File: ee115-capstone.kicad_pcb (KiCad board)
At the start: 2 copper layers, 122 parts, among them J1 2171790001, J2 9V_BATTERY, J3 Conn_01x04_Pin, J5 Conn_01x03_Pin, J6 Conn_02x02_Odd_Even, Q1 PMOS, Q2 NMOS, Q3 NPN, Q4 AO3400A, Q5 AO3400A, Q6 NMOS, SW1 SW_Push, SW2 SW_Push, SW3 SW_Push, U1 OPA2140AIDR, U10 SN74LVC1G02DCKR (NOR), U11 SN74LVC1G02DCKR (NOR), U12 ALD1107PBL, U13 MCP6571T-E/OT, U14 SL78L05, U15 300P14-U, U16 OPA705PA, U17 MIC4605-2YM-TR, U18 OPA705PA, U19 OPA705PA, U2 CD4052BPWR, U20 TLV9101IDBVR, U21 MCP6571T-E/OT, U3 LM393DR, U4 ADG601BRMZ-REEL7, U5 ESP32-C3-WROOM-02-N4, U6 AP2112K-3.3, U7 MCP601T-E_OT, U8 MCP6571T-E/OT, U9 MCP6571T-E/OT

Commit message: adc PCB
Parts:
- removed R8: 0, Resistor_SMD:R_0805_2012Metric
- added U13: MCP6571T-E/OT, footprints:SOP_MCP6571T-E&slash_OT_MCH, F.Cu at (113.8, 56.3)
- moved C4 111.4 mm to (156.8, 62.4), turned to 90 degrees
- moved R2 107.2 mm to (154.6, 67.0), turned to -90 degrees
- moved C2 105.3 mm to (151.5, 54.8)
- moved R3 104.5 mm to (154.7, 63.3), turned to -90 degrees
- moved C16 103.5 mm to (155.0, 59.5), turned to 180 degrees
- moved J6 100.8 mm to (154.2, 75.1), turned to -90 degrees
- moved U1 100.1 mm to (149.2, 63.8)
- moved D1 98.9 mm to (155.8, 54.8), turned to 90 degrees
- moved U4 98.8 mm to (136.6, 63.0), turned to 90 degrees
- moved R1 97.2 mm to (144.1, 62.5), turned to -90 degrees
- moved C6 92.2 mm to (139.4, 54.5), turned to 90 degrees
- moved J1 90.7 mm to (154.4, 46.0), turned to 90 degrees
- moved R10 90.6 mm to (151.8, 52.2), turned to 180 degrees
- moved J5 90.0 mm to (126.2, 29.5), turned to 180 degrees
- moved R9 87.5 mm to (151.7, 39.6), turned to 180 degrees
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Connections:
- C23 pad 1: +3V3 -> /LDO/+3.3V
- C24 pad 1: +3V3 -> /LDO/+3.3V
- Q6 pad 3: +3V3 -> /LDO/+3.3V
- R36 pad 1: +3V3 -> /LDO/+3.3V
- R38 pad 1: +3V3 -> /LDO/+3.3V
- U19 pad 7: unconnected-(U19-V+-Pad7) -> +9V
- U21 pad 6: (no net) -> +5V
- U5 pad 10: /ADC-MCU/COMP_OUT -> /ADC-MCU/MUX_B
- U5 pad 11: /ADC-MCU/MUX_B -> /ADC-MCU/MUX_A
- U5 pad 17: /ADC-MCU/ESP_ADC_2 -> /Thermistor
- U5 pad 6: /ADC-MCU/MUX_A -> /ADC-MCU/COMP_OUT
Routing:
- net 1.65V: track 0.00 -> 62.9 mm
- net /Thermopile: track 0.00 -> 56.4 mm, vias 0 -> 2
- net /Thermistor: track 0.00 -> 39.8 mm, vias 0 -> 1
- net /ADC-MCU/ESP_ADC_1: track 0.00 -> 29.3 mm, vias 0 -> 2
- net GND: track 0.00 -> 26.8 mm, vias 0 -> 5
- net Net-(U1-OUTA): track 0.00 -> 26.3 mm, vias 0 -> 2
- net /ADC-MCU/SCL: track 0.00 -> 19.0 mm
- net /ADC-MCU/COMP_OUT_BAR: track 0.00 -> 18.9 mm, vias 0 -> 2
- net /ADC-MCU/SDA: track 0.00 -> 18.8 mm
- net /ADC-MCU/BOOT: track 0.00 -> 17.8 mm, vias 0 -> 1
- net +3V3: track 0.00 -> 17.3 mm, vias 0 -> 3
- net /ADC-MCU/-VREF: track 0.00 -> 16.5 mm
- net /RANGE_SEL: track 0.00 -> 16.1 mm
- net Net-(U1-INA-): track 0.00 -> 15.7 mm
- net /ADC-MCU/EN: track 0.00 -> 14.0 mm
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- added copper zone on F.Cu, net +5V
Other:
- copper layers 2 -> 4

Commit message: pcb layout
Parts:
- removed U13 (x2): MCP6571T-E/OT, footprints:SOP_MCP6571T-E&slash_OT_MCH
- added C25: C_Polarized, Capacitor_SMD:C_0805_2012Metric, F.Cu at (179.7, 109.5)
- added C26: C_Polarized, Capacitor_SMD:C_0805_2012Metric, F.Cu at (171.3, 183.9)
- added C27: C_Polarized, Capacitor_SMD:C_0805_2012Metric, F.Cu at (171.3, 180.9)
- added C28: C_Polarized, Capacitor_SMD:C_0805_2012Metric, F.Cu at (171.4, 178.0)
- added C29: C_Polarized, Capacitor_SMD:C_0805_2012Metric, F.Cu at (171.4, 175.2)
- added C30: C_Polarized, Capacitor_SMD:C_0805_2012Metric, F.Cu at (158.3, 162.8)
- added C31: C_Polarized, Capacitor_SMD:C_0805_2012Metric, F.Cu at (158.3, 165.7)
- added C32: C_Polarized, Capacitor_SMD:C_0805_2012Metric, F.Cu at (158.3, 168.5)
- added C33: C_Polarized, Capacitor_SMD:C_0805_2012Metric, F.Cu at (158.3, 171.4)
- added C34: C_Polarized, Capacitor_SMD:C_0805_2012Metric, F.Cu at (154.7, 161.3)
- added C35: C_Polarized, Capacitor_SMD:C_0805_2012Metric, F.Cu at (154.7, 164.2)
- added C36: C_Polarized, Capacitor_SMD:C_0805_2012Metric, F.Cu at (154.7, 167.0)
- added C37: C_Polarized, Capacitor_SMD:C_0805_2012Metric, F.Cu at (154.7, 169.9)
- added C38: C_Polarized, Capacitor_SMD:C_0805_2012Metric, F.Cu at (137.7, 164.0)
- added C39: C_Polarized, Capacitor_SMD:C_0805_2012Metric, F.Cu at (161.9, 173.2)
- added C40: C_Polarized, Capacitor_SMD:C_0805_2012Metric, F.Cu at (146.8, 157.8)
- added C41: C_Polarized, Capacitor_SMD:C_0805_2012Metric, F.Cu at (88.5, 181.2)
- added C42: C_Polarized, Capacitor_SMD:C_0805_2012Metric, F.Cu at (153.4, 151.8)
- added C43: C_Polarized, Capacitor_SMD:C_0805_2012Metric, F.Cu at (88.5, 187.2)
- added C44: C_Polarized, Capacitor_SMD:C_0805_2012Metric, F.Cu at (88.5, 190.2)
- added C45: C_Polarized, Capacitor_SMD:C_0805_2012Metric, F.Cu at (147.8, 115.6)
- added C46: C_Polarized, Capacitor_SMD:C_0805_2012Metric, F.Cu at (95.0, 192.2)
- added C47: C_Polarized, Capacitor_SMD:C_0805_2012Metric, F.Cu at (95.0, 195.2)
- added C48: C_Polarized, Capacitor_SMD:C_0805_2012Metric, F.Cu at (143.3, 178.1)
- added C49: C_Polarized, Capacitor_SMD:C_0805_2012Metric, F.Cu at (140.0, 178.1)
- added D4: D_Schottky, Diode_SMD:D_SOD-523, F.Cu at (165.4, 148.1)
- added Q7: PNP, Package_TO_SOT_THT:TO-220F-3_Vertical, F.Cu at (166.6, 155.6)
- added Q8: NPN, Package_TO_SOT_THT:TO-220-3_Horizontal_TabDown, F.Cu at (175.3, 104.7)
- added R30: R, Resistor_SMD:R_0805_2012Metric, F.Cu at (166.9, 176.3)
- added R42: R, Resistor_SMD:R_0805_2012Metric, F.Cu at (166.7, 150.1)
- added R43: R, Resistor_SMD:R_0805_2012Metric, F.Cu at (172.2, 160.8)
- added R44: R, Resistor_SMD:R_0805_2012Metric, F.Cu at (172.2, 157.2)
- added R45: R, Resistor_SMD:R_0805_2012Metric, F.Cu at (176.4, 108.3)
- added R46: R, Resistor_SMD:R_0805_2012Metric, F.Cu at (162.7, 183.9)
- added R47: R, Resistor_SMD:R_0805_2012Metric, F.Cu at (162.7, 180.9)
- added R48: R, Resistor_SMD:R_0805_2012Metric, F.Cu at (162.7, 178.0)
- added R50: R, Resistor_SMD:R_0805_2012Metric, F.Cu at (162.7, 186.8)
- added R51: R, Resistor_SMD:R_0805_2012Metric, F.Cu at (158.4, 185.4)
- added R52: R, Resistor_SMD:R_0805_2012Metric, F.Cu at (158.4, 183.0)
- added R53: R, Resistor_SMD:R_0805_2012Metric, F.Cu at (158.4, 180.7)
- added R54: R, Resistor_SMD:R_0805_2012Metric, F.Cu at (158.4, 178.3)
- added R8: R, Resistor_SMD:R_0805_2012Metric, F.Cu at (162.8, 153.5)
- added Re1: R, Resistor_SMD:R_0805_2012Metric, F.Cu at (161.8, 161.3)
- added Re2: R, Resistor_SMD:R_0805_2012Metric, F.Cu at (161.8, 164.2)
- added Re3: R, Resistor_SMD:R_0805_2012Metric, F.Cu at (161.8, 167.0)
- added Re4: R, Resistor_SMD:R_0805_2012Metric, F.Cu at (161.8, 169.9)
- added TP19: TestPoint, TestPoint:TestPoint_Plated_Hole_D2.0mm, F.Cu at (146.4, 151.1)
- added TP20: TestPoint, TestPoint:TestPoint_Plated_Hole_D2.0mm, F.Cu at (142.8, 149.2)
- added TP21: TestPoint, TestPoint:TestPoint_Plated_Hole_D2.0mm, F.Cu at (148.5, 154.1)
- added TP22: TestPoint, TestPoint:TestPoint_Plated_Hole_D2.0mm, F.Cu at (144.2, 145.7)
- added TP23: TestPoint, TestPoint:TestPoint_Plated_Hole_D2.0mm, F.Cu at (165.4, 143.0)
- added TP24: TestPoint, TestPoint:TestPoint_Plated_Hole_D2.0mm, F.Cu at (139.5, 151.9)
- added TP26: TestPoint, TestPoint:TestPoint_Plated_Hole_D2.0mm, F.Cu at (159.2, 154.2)
- Q3: footprint Package_TO_SOT_THT:TO-220-3_Horizontal_TabDown -> Package_TO_SOT_THT:TO-220-3_Vertical
- TP1, TP2, TP3, TP4, TP5, TP6, TP7, TP8: footprint Connector_Pin:Pin_D1.0mm_L10.0mm -> TestPoint:TestPoint_Plated_Hole_D2.0mm
- TP10, TP11, TP12, TP13, TP14, TP15, TP16, TP17, TP18, TP9: footprint TestPoint:TestPoint_Pad_D1.0mm -> TestPoint:TestPoint_Plated_Hole_D2.0mm
- U10, U11: footprint footprints:DCK0005A_N -> footprints_pretty:DCK0005A_N
- U20: value TLV9101IDBVR -> AD8038; footprint footprints:DBV0005A_TEX -> footprints_pretty:KS_5_ADI
- moved R27 160.2 mm to (166.9, 188.5), turned to 180 degrees
- moved TP15 155.4 mm to (162.7, 189.8)
- moved C20 153.5 mm to (171.3, 186.8), turned to 180 degrees
- moved R28 152.4 mm to (158.4, 187.7), turned to 180 degrees
- moved R31 147.7 mm to (166.9, 185.2), turned to 180 degrees
- moved R32 143.0 mm to (167.0, 182.2), turned to 180 degrees
- moved R29 142.2 mm to (162.7, 175.5), turned to 180 degrees
- moved R33 138.4 mm to (166.9, 179.3), turned to 180 degrees
- moved U16 138.3 mm to (222.5, 105.1)
- moved R35 137.1 mm to (211.0, 102.5), turned to 180 degrees
- moved U15 136.8 mm to (203.7, 107.8)
- moved TP16 134.1 mm to (154.1, 173.2)
- moved U12 133.9 mm to (185.1, 99.0)
- moved R26 132.8 mm to (148.1, 165.1), turned to 90 degrees
- moved TP18 131.7 mm to (146.8, 180.7), turned to -90 degrees
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- renumbered R30 to R67
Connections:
- C23 pad 1: /LDO/+3.3V -> +3V3
- C24 pad 1: /LDO/+3.3V -> +3V3
- C9 pad 1: /Buck Converter/Sawtooth Generator/sawtooth -> /Buck Converter/Sawtooth Generator/saw
- Q3 pad 1: /Buck Converter/I_PTAT -> Net-(Q3-C)
- Q6 pad 3: /LDO/+3.3V -> +3V3
- R21 pad 1: /Buck Converter/I_PTAT -> Net-(Q3-C)
- R21 pad 2: /Buck Converter/Sawtooth Generator/sawtooth -> /Buck Converter/Sawtooth Generator/saw
- R36 pad 1: /LDO/+3.3V -> +3V3
- R38 pad 1: /LDO/+3.3V -> +3V3
- TP14 pad 1: /Buck Converter/Sawtooth Generator/sawtooth -> /Buck Converter/Sawtooth Generator/saw
- U12 pad 12: +9V -> /bandgap/pwr_bus
- U12 pad 3: +9V -> /bandgap/pwr_bus
- U12 pad 7: +9V -> /bandgap/pwr_bus
- U12 pad 8: +9V -> /bandgap/pwr_bus
- U16 pad 7: +9V -> /bandgap/pwr_bus
- U18 pad 2: /LDO/volt_ref -> /Buck Converter/bg_volt
- U18 pad 6: /LDO/volt_ref -> /Buck Converter/bg_volt
- U18 pad 7: +9V -> /bandgap/pwr_bus
- U19 pad 3: /LDO/volt_ref -> /Buck Converter/bg_volt
- U20 pad 3: unconnected-(U20-+-Pad3) -> /Buck Converter/bg_volt
- U21 pad 4: /Buck Converter/Sawtooth Generator/sawtooth -> /Buck Converter/Sawtooth Generator/saw
- U8 pad 3: /Buck Converter/Sawtooth Generator/unprocessed_saw -> /Buck Converter/Sawtooth Generator/saw
- U9 pad 4: /Buck Converter/Sawtooth Generator/unprocessed_saw -> /Buck Converter/Sawtooth Generator/saw
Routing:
- net /Buck Converter/Sawtooth Generator/out_Q_not: track 0.00 -> 26.4 mm
- net Net-(C22-Pad2): track 0.00 -> 25.9 mm
- net /Buck Converter/Sawtooth Generator/saw: track 0.00 -> 11.2 mm
- net Net-(U8--): track 0.00 -> 10.4 mm
- net Net-(U11-A): track 0.00 -> 9.43 mm
- net Net-(U10-A): track 0.00 -> 8.32 mm
- net Net-(U9-+): track 0.00 -> 7.83 mm
- net Net-(D4-A): track 0.00 -> 4.86 mm
- net Net-(Q3-C): track 0.00 -> 2.01 mm
- added copper zone on F.Cu, net /Buck Converter/Sawtooth Generator/saw

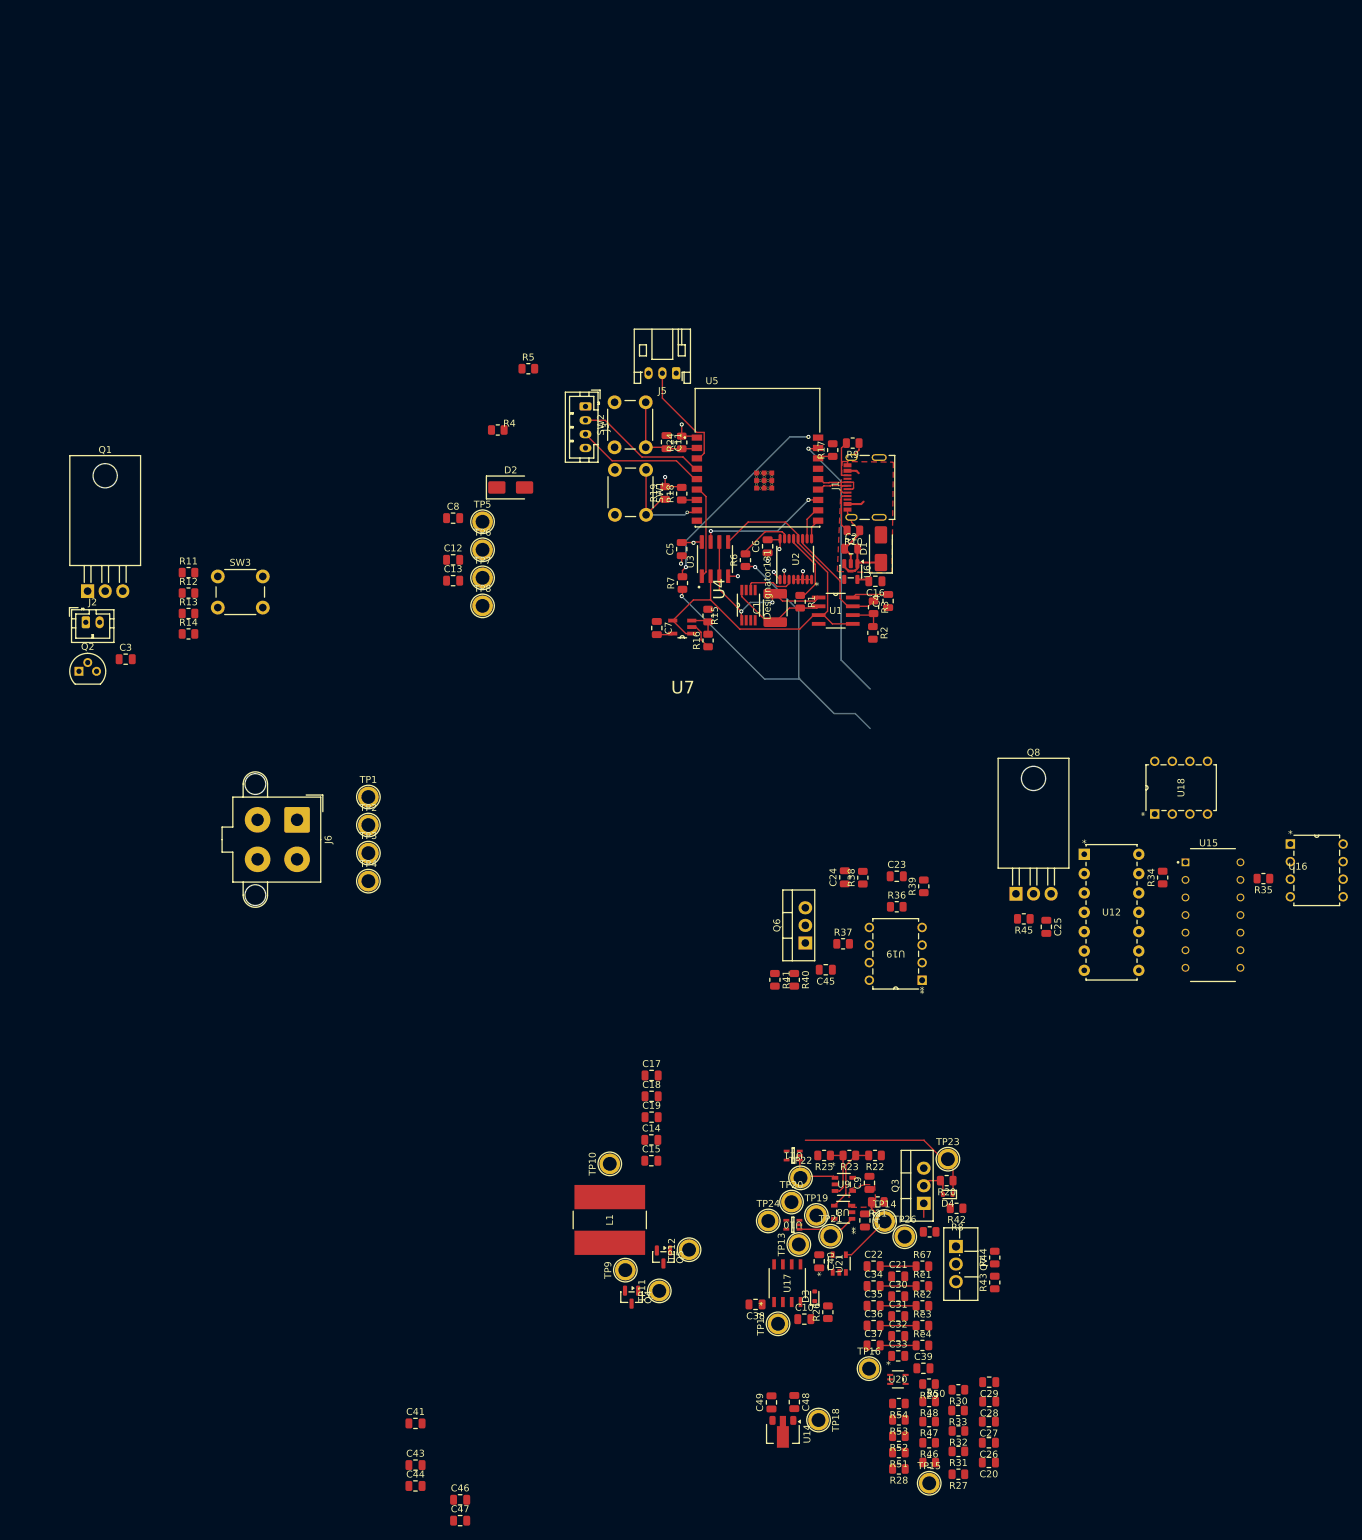
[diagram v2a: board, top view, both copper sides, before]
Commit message: pcb layout component placement 90% done
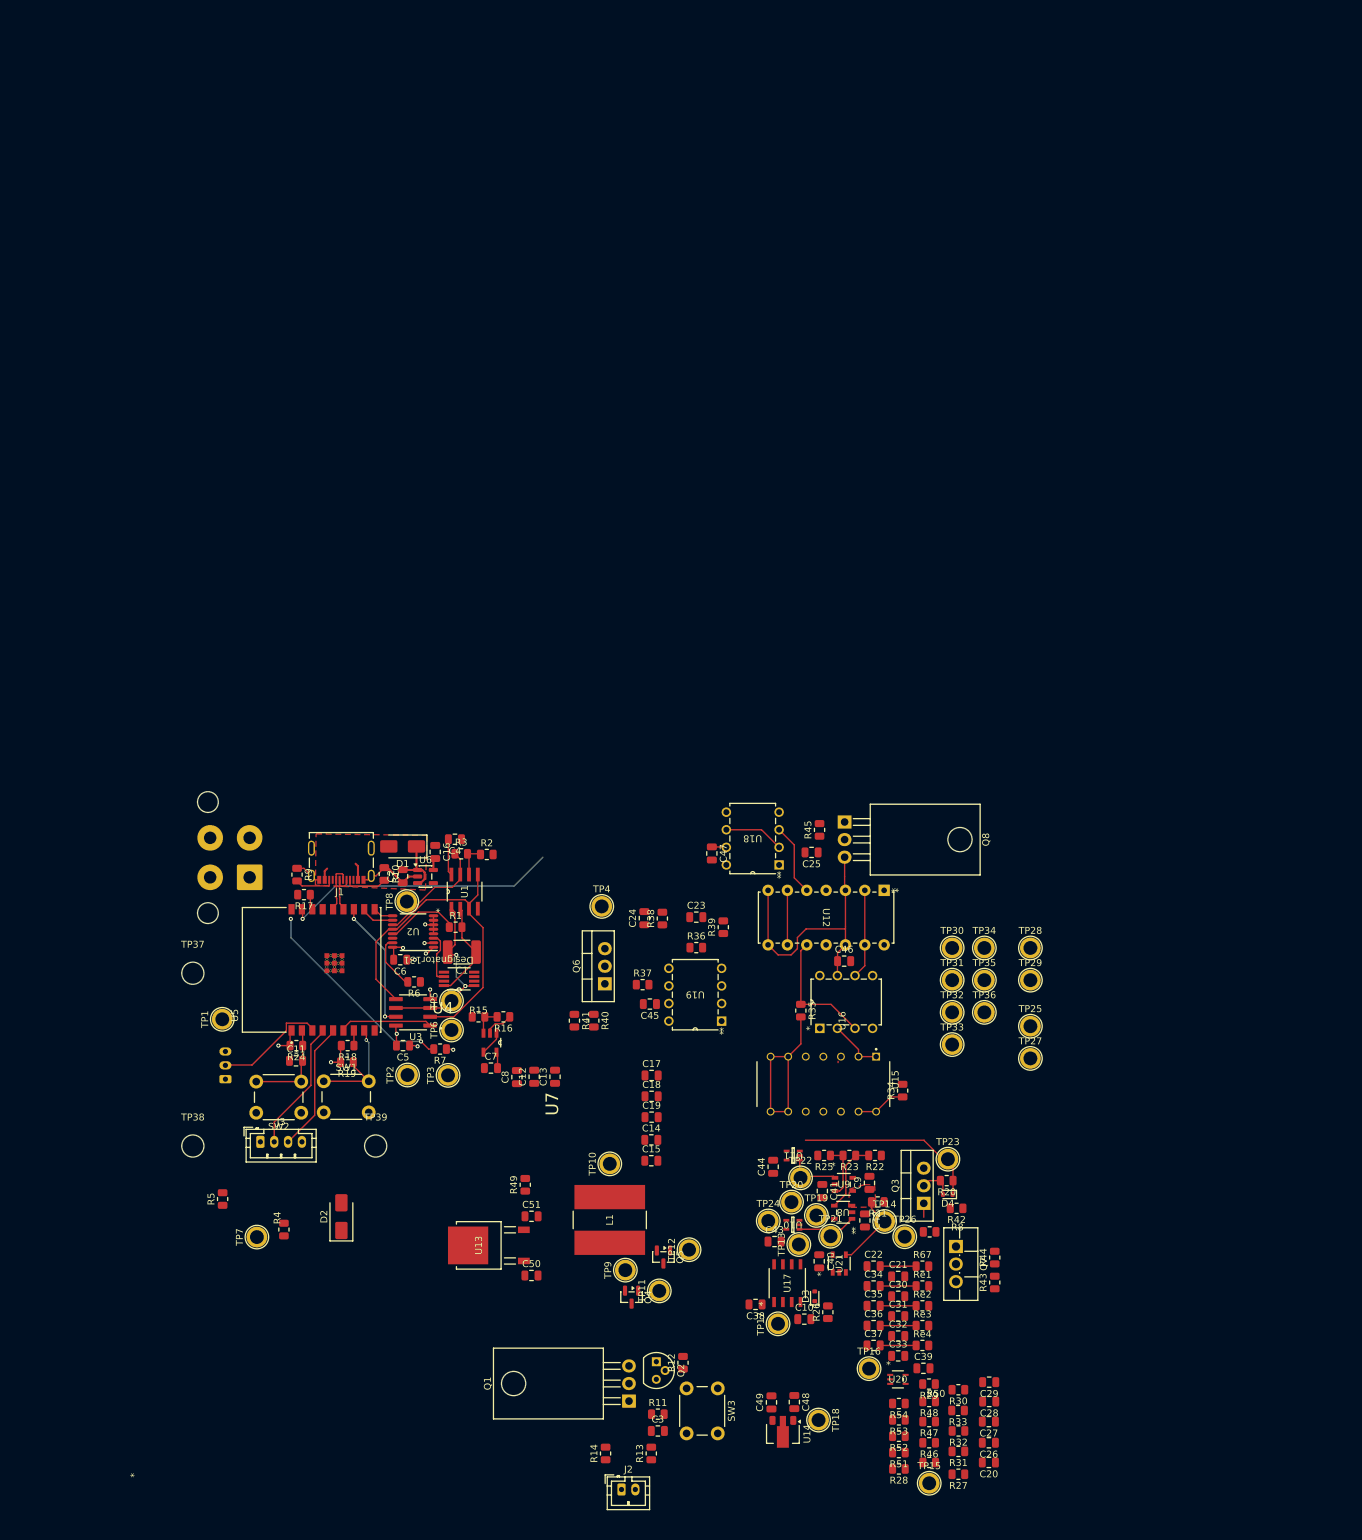
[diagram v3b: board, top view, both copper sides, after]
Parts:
- added C50: C, Capacitor_SMD:C_0805_2012Metric, F.Cu at (105.3, 159.8)
- added C51: C, Capacitor_SMD:C_0805_2012Metric, F.Cu at (105.3, 151.2)
- added R49: 0, Resistor_SMD:R_0805_2012Metric, F.Cu at (104.4, 146.7)
- added TP25: TestPoint, TestPoint:TestPoint_Plated_Hole_D2.0mm, F.Cu at (177.3, 123.8)
- added TP27: TestPoint, TestPoint:TestPoint_Plated_Hole_D2.0mm, F.Cu at (177.3, 128.4)
- added TP28: TestPoint, TestPoint:TestPoint_Plated_Hole_D2.0mm, F.Cu at (177.3, 112.5)
- added TP29: TestPoint, TestPoint:TestPoint_Plated_Hole_D2.0mm, F.Cu at (177.3, 117.2)
- added TP30: TestPoint, TestPoint:TestPoint_Plated_Hole_D2.0mm, F.Cu at (166.1, 112.5)
- added TP31: TestPoint, TestPoint:TestPoint_Plated_Hole_D2.0mm, F.Cu at (166.1, 117.2)
- added TP32: TestPoint, TestPoint:TestPoint_Plated_Hole_D2.0mm, F.Cu at (166.1, 121.8)
- added TP33: TestPoint, TestPoint:TestPoint_Plated_Hole_D2.0mm, F.Cu at (166.1, 126.5)
- added TP34: TestPoint, TestPoint:TestPoint_Plated_Hole_D2.0mm, F.Cu at (170.7, 112.5)
- added TP35: TestPoint, TestPoint:TestPoint_Plated_Hole_D2.0mm, F.Cu at (170.7, 117.2)
- added TP36: TestPoint, TestPoint:TestPoint_Plated_Hole_D2.0mm, F.Cu at (170.7, 121.8)
- added TP37: TestPoint, MountingHole:MountingHole_3.2mm_M3, F.Cu at (56.4, 116.2)
- added TP38: TestPoint, MountingHole:MountingHole_3.2mm_M3, F.Cu at (56.4, 141.1)
- added TP39: TestPoint, MountingHole:MountingHole_3.2mm_M3, F.Cu at (82.8, 141.1)
- added U13: LD39150DT33-R, footprints_pretty:SOT_0DT33-R_STM, F.Cu at (97.7, 155.4)
- J5, J6: moved to B.Cu
- moved J2 147.2 mm to (118.3, 190.7)
- moved Q1 140.7 mm to (119.4, 177.9), turned to 90 degrees
- moved R11 139.1 mm to (123.5, 179.8)
- moved R13 138.5 mm to (122.6, 185.5), turned to 90 degrees
- moved SW3 137.7 mm to (132.2, 176.1), turned to -90 degrees
- moved C3 135.4 mm to (123.5, 182.2)
- moved R14 132.8 mm to (116.0, 185.5), turned to 90 degrees
- moved R12 132.1 mm to (127.2, 172.4), turned to 90 degrees
- moved Q2 130.0 mm to (123.3, 172.2), turned to -90 degrees
- moved R5 127.8 mm to (60.7, 148.8), turned to 90 degrees
- moved J5 121.0 mm to (61.1, 131.4), turned to 90 degrees
- moved R4 119.5 mm to (69.5, 153.2), turned to 90 degrees
- moved J3 116.1 mm to (66.2, 140.5), turned to 0 degrees
- moved D2 108.1 mm to (77.8, 151.3), turned to 90 degrees
- moved SW2 106.2 mm to (72.0, 136.3), turned to 180 degrees
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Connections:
- U12 pad 11: unconnected-(U12-V+-Pad11) -> /bandgap/pwr_bus
- U15 pad 1: Net-(R34-Pad1) -> /bandgap/minus
- U15 pad 13: /bandgap/collect -> Net-(R34-Pad1)
- U15 pad 14: /bandgap/collect -> Net-(R34-Pad1)
- U15 pad 2: Net-(R34-Pad1) -> /bandgap/minus
- U15 pad 6: /bandgap/minus -> /bandgap/collect
- U15 pad 7: /bandgap/minus -> /bandgap/collect
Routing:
- net /Thermopile: track 56.4 -> 1.03 mm, vias 2 -> 1
- net /bandgap/pwr_bus: track 0.00 -> 41.7 mm
- net /bandgap/collect: track 0.00 -> 27.6 mm
- net /bandgap/feed: track 0.00 -> 20.8 mm
- net /bandgap/plus: track 0.00 -> 18.2 mm
- net /bandgap/vref: track 0.00 -> 10.4 mm
- net /Buck Converter/bg_volt: track 0.00 -> 8.67 mm
- net /bandgap/minus: track 0.00 -> 7.89 mm
- net Net-(R34-Pad1): track 0.00 -> 7.25 mm
- net 1.65V: track 62.9 -> 56.2 mm
- net /ADC-MCU/ESP_ADC_1: track 29.3 -> 30.0 mm

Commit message: init pcb
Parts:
- removed C50, C51: C, Capacitor_SMD:C_0805_2012Metric
- removed J6: Conn_02x02_Odd_Even, Connector_Molex:Molex_Mega-Fit_76829-0004_2x02_P5.70mm_Vertical
- removed R14, R49: 0, Resistor_SMD:R_0805_2012Metric
- removed TP10, TP11, TP12, TP25, TP27, TP28, TP29, TP30, TP31, TP32, TP33, TP34, TP35, TP36, TP4, TP9: TestPoint, TestPoint:TestPoint_Plated_Hole_D2.0mm
- removed U13: LD39150DT33-R, footprints_pretty:SOT_0DT33-R_STM
- added J4: Conn_01x04_Pin, Connector_Molex:Molex_KK-254_AE-6410-04A_1x04_P2.54mm_Vertical, F.Cu at (60.6, 100.5)
- added SW4: GF-123-0054, footprints:SW2_GF-123-0054_CWI, F.Cu at (130.1, 100.4)
- moved J2 93.7 mm to (119.6, 97.0)
- moved R13 84.0 mm to (118.8, 101.6), turned to 0 degrees
- moved Q1 81.8 mm to (111.9, 96.5), turned to 180 degrees
- moved C3 79.9 mm to (121.7, 102.4), turned to -90 degrees
- moved R11 77.4 mm to (124.2, 102.4), turned to -90 degrees
- moved U14 69.9 mm to (172.3, 119.9), turned to 90 degrees
- moved SW3 68.6 mm to (126.5, 107.7)
- moved C49 67.6 mm to (176.1, 121.0)
- moved R34 66.7 mm to (92.3, 128.9), turned to 0 degrees
- moved Q2 65.7 mm to (118.1, 106.8), turned to 90 degrees
- moved R12 63.3 mm to (117.5, 109.8), turned to 0 degrees
- moved C48 62.5 mm to (168.5, 120.9)
- moved L1 59.0 mm to (161.4, 113.4), turned to 180 degrees
- moved U15 58.4 mm to (89.6, 140.3), turned to 0 degrees
- moved C46 57.0 mm to (102.2, 144.8), turned to -90 degrees
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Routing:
- net +9V: track 0.00 -> 134.2 mm, vias 0 -> 2
- net Net-(U20--): track 0.00 -> 78.8 mm
- net /POWER_LATCH: track 0.00 -> 73.8 mm, vias 0 -> 1
- net /Buck Converter/I_PTAT: track 0.00 -> 63.9 mm
- net /bandgap/minus: track 7.89 -> 55.5 mm
- net /Buck Converter/error: track 0.00 -> 41.9 mm
- net +3.5V: track 0.00 -> 38.4 mm
- net GND: track 26.8 -> 64.9 mm
- net /Buck Converter/bg_volt: track 8.67 -> 46.3 mm, vias 0 -> 1
- net /Thermopile: track 1.03 -> 34.5 mm
- net Net-(Q1-G): track 0.00 -> 29.4 mm
- net /Buck Converter/switch_node: track 0.00 -> 28.0 mm
- net Net-(C20-Pad2): track 0.00 -> 27.5 mm
- net /bandgap/pwr_bus: track 41.7 -> 66.4 mm
- net /Thermistor: track 39.8 -> 15.8 mm
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- added copper zone on F.Cu, net +9V
- added copper zone on In1.Cu, net GND
